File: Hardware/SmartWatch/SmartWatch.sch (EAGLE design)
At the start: 44 parts, among them U1 STM32L476, U3 UG-2828GDEDF11, U4 FAN5331SX, U5 APDS-9960, U6 LTC3557

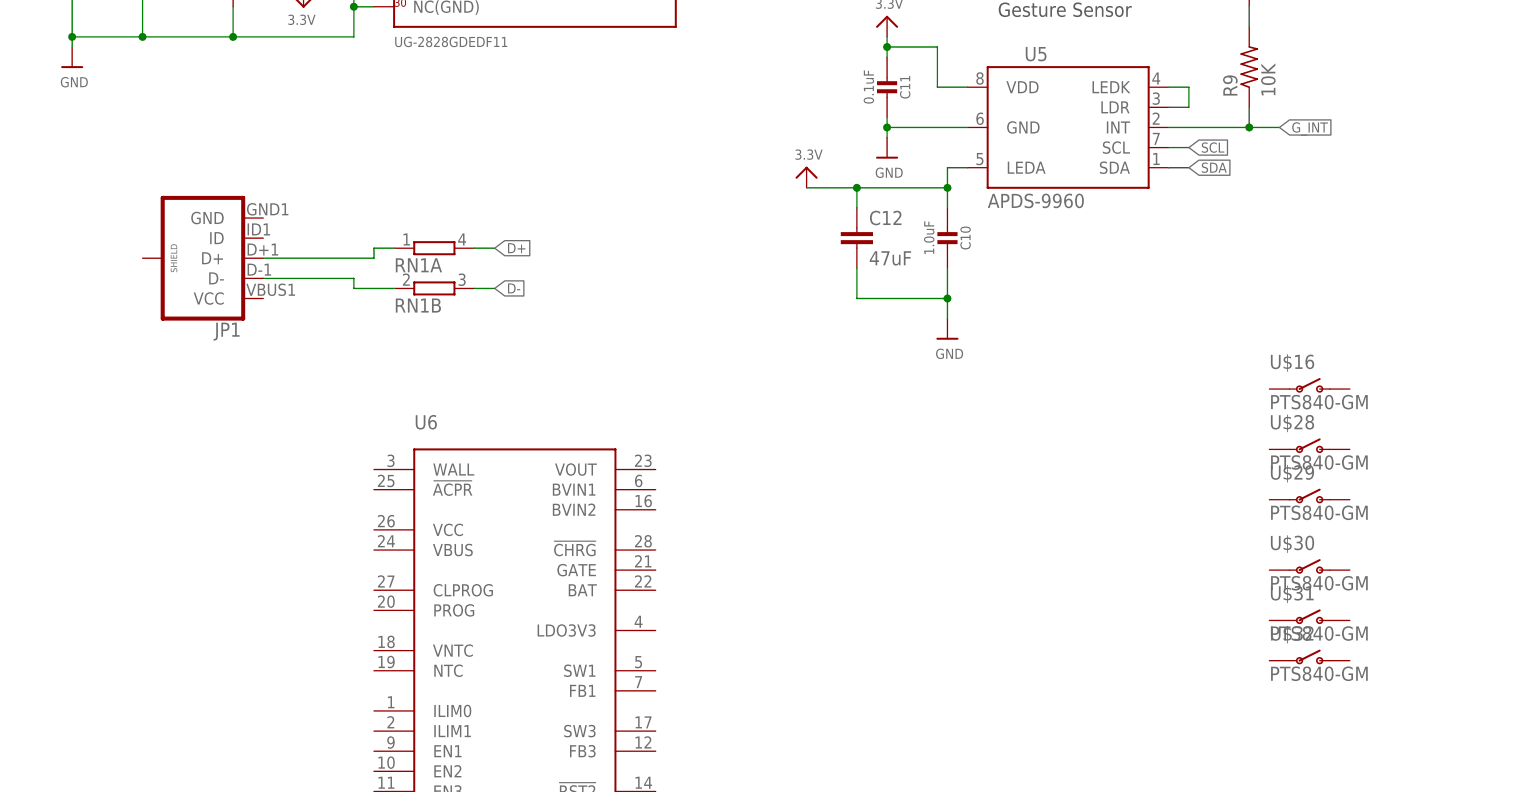
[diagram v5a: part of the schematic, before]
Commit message: created usb part
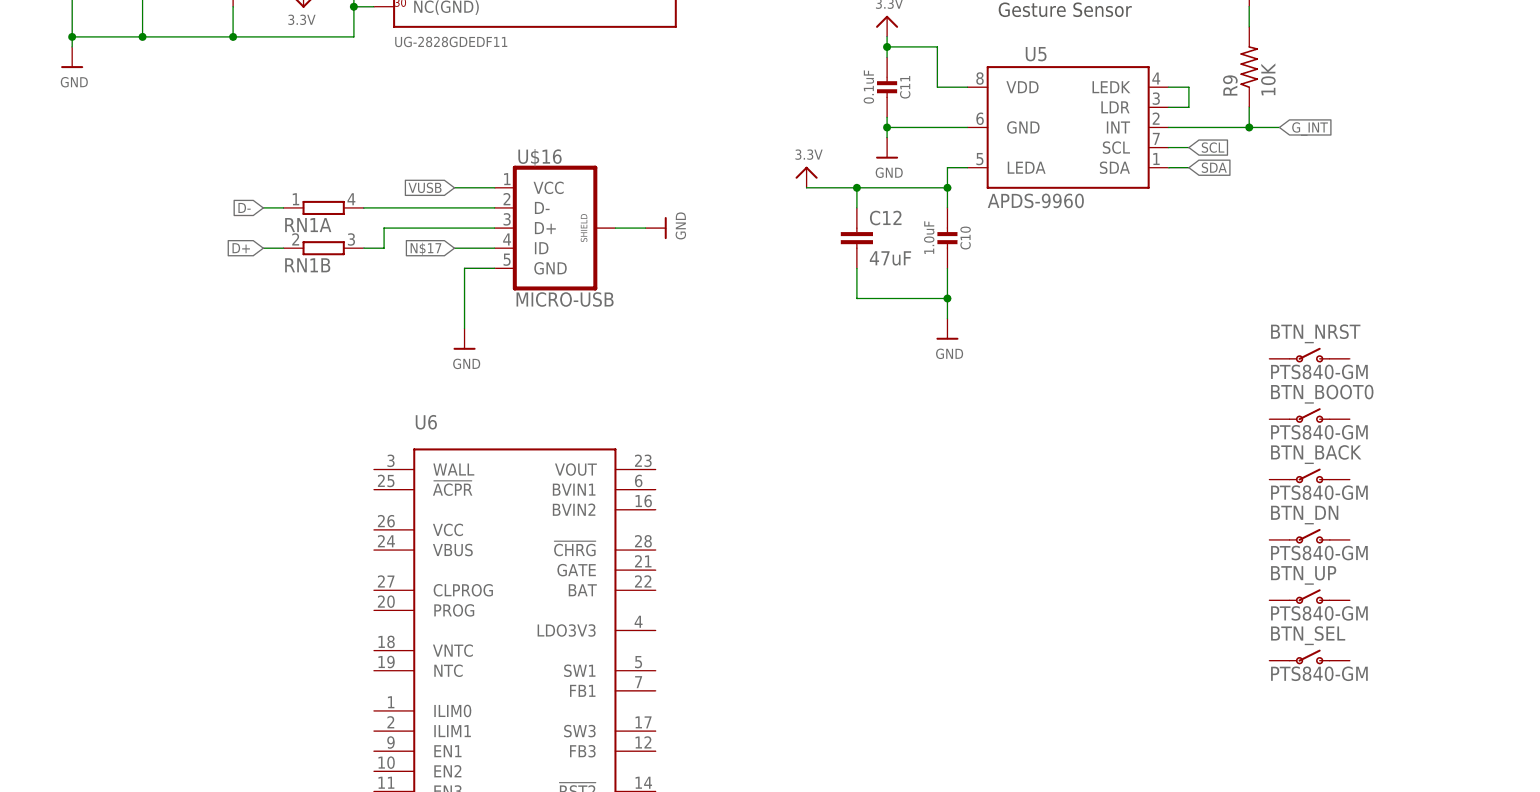
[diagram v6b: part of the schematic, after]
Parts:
- removed JP1: (no value), SparkFun-Connectors:USB_MICROB_PLUGCONN-11752
- removed U$28, U$29, U$30, U$31: PTS840-GM, SmartWatch:PTS840-GM
- added BTN_BACK, BTN_BOOT0, BTN_DN, BTN_NRST, BTN_UP: PTS840-GM, SmartWatch:PTS840-GM
- U$16: value PTS840-GM -> MICRO-USB; device SmartWatch:PTS840-GM -> SmartWatch:MICRO-USB
- renumbered U$32 to BTN_SEL
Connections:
- removed net N$10: JP1.D+, RN1A.1
- new net ID: RN1B.2, U$16.D+
- new net N$17: U$16.ID
- new net VUSB: U$16.VCC
- net D+: now also RN1B.1; no longer RN1A.2
- net D-: now also RN1A.1; no longer RN1B.2
- net GND: now also U$16.GND, U$16.SHIELD
- net N$15: now also RN1A.2, U$16.D-; no longer JP1.D-, RN1B.1
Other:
- moved on the sheet: RN1A, RN1B
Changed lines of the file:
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@@
 <part name="C1" library="microbuilder" deviceset="CAP_CERAMIC" device="0603MINI" value="1uF"/>
 <part name="U6" library="SmartWatch" deviceset="LTC3557" device=""/>
-<part name="JP1" library="SparkFun-Connectors" deviceset="USB_MICROB_PLUG" device="CONN-11752"/>
+<part name="U$27" library="supply1" deviceset="+12V" device="" value="+13V"/>
+<part name="BTN_NRST" library="SmartWatch" deviceset="PTS840-GM" device=""/>
+<part name="BTN_BOOT0" library="SmartWatch" deviceset="PTS840-GM" device=""/>
+<part name="BTN_BACK" library="SmartWatch" deviceset="PTS840-GM" device=""/>
+<part name="BTN_DN" library="SmartWatch" deviceset="PTS840-GM" device=""/>
+<part name="BTN_UP" library="SmartWatch" deviceset="PTS840-GM" device=""/>
+<part name="BTN_SEL" library="SmartWatch" deviceset="PTS840-GM" device=""/>
+<part name="U$16" library="SmartWatch" deviceset="MICRO-USB" device=""/>
+<part name="U$28" library="microbuilder" deviceset="GND" device=""/>
+<part name="U$29" library="microbuilder" deviceset="GND" device=""/>
 <part name="RN1" library="MicroBoard" deviceset="2R-N" device="EXBV4V"/>
-<part name="U$27" library="supply1" deviceset="+12V" device="" value="+13V"/>
-<part name="U$16" library="SmartWatch" deviceset="PTS840-GM" device=""/>
-<part name="U$28" library="SmartWatch" deviceset="PTS840-GM" device=""/>
-<part name="U$29" library="SmartWatch" deviceset="PTS840-GM" device=""/>
-<part name="U$30" library="SmartWatch" deviceset="PTS840-GM" device=""/>
-<part name="U$31" library="SmartWatch" deviceset="PTS840-GM" device=""/>
-<part name="U$32" library="SmartWatch" deviceset="PTS840-GM" device=""/>
 </parts>
 <sheets>
@@
 <instance part="C1" gate="G$1" x="13.97" y="69.85" rot="R180"/>
 <instance part="U6" gate="G$1" x="198.12" y="-48.26"/>
-<instance part="JP1" gate="G$1" x="158.75" y="1.27" rot="R180"/>
-<instance part="RN1" gate="A" x="187.96" y="2.54"/>
-<instance part="RN1" gate="B" x="187.96" y="-2.54"/>
 <instance part="U$27" gate="1" x="298.45" y="92.71"/>
-<instance part="U$16" gate="G$1" x="298.45" y="-15.24"/>
-<instance part="U$28" gate="G$1" x="298.45" y="-22.86"/>
-<instance part="U$29" gate="G$1" x="298.45" y="-29.21"/>
-<instance part="U$30" gate="G$1" x="298.45" y="-38.1"/>
-<instance part="U$31" gate="G$1" x="298.45" y="-44.45"/>
-<instance part="U$32" gate="G$1" x="298.45" y="-49.53"/>
+<instance part="BTN_NRST" gate="G$1" x="298.45" y="-11.43"/>
+<instance part="BTN_BOOT0" gate="G$1" x="298.45" y="-19.05"/>
+<instance part="BTN_BACK" gate="G$1" x="298.45" y="-26.67"/>
+<instance part="BTN_DN" gate="G$1" x="298.45" y="-34.29"/>
+<instance part="BTN_UP" gate="G$1" x="298.45" y="-41.91"/>
+<instance part="BTN_SEL" gate="G$1" x="298.45" y="-49.53"/>
+<instance part="U$16" gate="G$1" x="203.2" y="5.08"/>
+<instance part="U$28" gate="G$1" x="217.17" y="5.08" rot="R90"/>
+<instance part="U$29" gate="G$1" x="191.77" y="-10.16"/>
+<instance part="RN1" gate="A" x="173.99" y="7.62"/>
+<instance part="RN1" gate="B" x="173.99" y="2.54"/>
 </instances>
 <busses>
@@
 <pinref part="C12" gate="G$1" pin="2"/>
 </segment>
+<segment>
+<pinref part="U$28" gate="G$1" pin="GND"/>
+<pinref part="U$16" gate="G$1" pin="SHIELD"/>
+<wire x1="214.63" y1="5.08" x2="210.82" y2="5.08" width="0.1524" layer="91"/>
+</segment>
+<segment>
+<pinref part="U$16" gate="G$1" pin="GND"/>
+<wire x1="195.58" y1="0" x2="191.77" y2="0" width="0.1524" layer="91"/>
+<wire x1="191.77" y1="0" x2="191.77" y2="-7.62" width="0.1524" layer="91"/>
+<pinref part="U$29" gate="G$1" pin="GND"/>
+</segment>
 </net>
 <net name="BT_SCK" class="0">
@@
 </segment>
 </net>
-<net name="N$10" class="0">
-<segment>
-<pinref part="JP1" gate="G$1" pin="D+"/>
-<wire x1="166.37" y1="1.27" x2="180.34" y2="1.27" width="0.1524" layer="91"/>
-<wire x1="180.34" y1="1.27" x2="180.34" y2="2.54" width="0.1524" layer="91"/>
+<net name="VUSB" class="0">
+<segment>
+<pinref part="U$16" gate="G$1" pin="VCC"/>
+<wire x1="195.58" y1="10.16" x2="190.5" y2="10.16" width="0.1524" layer="91"/>
+<label x="190.5" y="10.16" size="1.27" layer="95" rot="R180" xref="yes"/>
+</segment>
+</net>
+<net name="N$15" class="0">
+<segment>
+<pinref part="U$16" gate="G$1" pin="D-"/>
+<pinref part="RN1" gate="A" pin="2"/>
+<wire x1="195.58" y1="7.62" x2="179.07" y2="7.62" width="0.1524" layer="91"/>
+</segment>
+</net>
+<net name="ID" class="0">
+<segment>
+<pinref part="U$16" gate="G$1" pin="D+"/>
+<wire x1="195.58" y1="5.08" x2="181.61" y2="5.08" width="0.1524" layer="91"/>
+<wire x1="181.61" y1="5.08" x2="181.61" y2="2.54" width="0.1524" layer="91"/>
+<pinref part="RN1" gate="B" pin="2"/>
+<wire x1="181.61" y1="2.54" x2="179.07" y2="2.54" width="0.1524" layer="91"/>
+</segment>
+</net>
+<net name="N$17" class="0">
+<segment>
+<pinref part="U$16" gate="G$1" pin="ID"/>
+<wire x1="195.58" y1="2.54" x2="190.5" y2="2.54" width="0.1524" layer="91"/>
+<label x="190.5" y="2.54" size="1.27" layer="95" rot="R180" xref="yes"/>
+</segment>
+</net>
+<net name="D-" class="0">
+<segment>
 <pinref part="RN1" gate="A" pin="1"/>
-<wire x1="180.34" y1="2.54" x2="182.88" y2="2.54" width="0.1524" layer="91"/>
-</segment>
-</net>
-<net name="N$15" class="0">
-<segment>
-<pinref part="JP1" gate="G$1" pin="D-"/>
-<wire x1="166.37" y1="-1.27" x2="177.8" y2="-1.27" width="0.1524" layer="91"/>
-<wire x1="177.8" y1="-1.27" x2="177.8" y2="-2.54" width="0.1524" layer="91"/>
+<wire x1="168.91" y1="7.62" x2="166.37" y2="7.62" width="0.1524" layer="91"/>
+<label x="166.37" y="7.62" size="1.27" layer="95" rot="R180" xref="yes"/>
+</segment>
+</net>
+<net name="D+" class="0">
+<segment>
 <pinref part="RN1" gate="B" pin="1"/>
-<wire x1="177.8" y1="-2.54" x2="182.88" y2="-2.54" width="0.1524" layer="91"/>
-</segment>
-</net>
-<net name="D+" class="0">
-<segment>
-<pinref part="RN1" gate="A" pin="2"/>
-<wire x1="193.04" y1="2.54" x2="195.58" y2="2.54" width="0.1524" layer="91"/>
-<label x="195.58" y="2.54" size="1.27" layer="95" xref="yes"/>
-</segment>
-</net>
-<net name="D-" class="0">
-<segment>
-<pinref part="RN1" gate="B" pin="2"/>
-<wire x1="193.04" y1="-2.54" x2="195.58" y2="-2.54" width="0.1524" layer="91"/>
-<label x="195.58" y="-2.54" size="1.27" layer="95" xref="yes"/>
-</segment>
-</net>
+<wire x1="168.91" y1="2.54" x2="166.37" y2="2.54" width="0.1524" layer="91"/>
+<label x="166.37" y="2.54" size="1.27" layer="95" rot="R180" xref="yes"/>
+</segment>
+</net>

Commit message: hardware updates
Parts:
- added C13, C15: 10uF, microbuilder:CAP_CERAMIC0603MINI
- added C16, C17: 2.2uF, microbuilder:CAP_CERAMIC0603MINI
- added R13, R14, R15, R16, R17, R18: 10K, resistor:R-US_R0603
- added R19: 2.5k, resistor:R-US_R0603
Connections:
- new net BNT_NRST: BTN_NRST.12, R13.2
- new net BTN_BACK: BTN_BACK.12, R15.2
- new net BTN_BOOT0: BTN_BOOT0.12, R14.2
- new net BTN_DN: BTN_DN.12, R16.2
- new net BTN_SEL: BTN_SEL.12, R18.2
- new net BTN_UP: BTN_UP.12, R17.2
- new net CHRG: U6.!CHRG
- new net N$10: RN1B.2, U$16.D-
- new net N$16: R19.2, U6.PROG
- new net N$19: C17.1, U6.BVIN1
- new net N$20: C16.1, U6.BVIN2
- new net VBAT: U6.BAT
- new net VOUT: C15.2, U6.VOUT
- net 3.3V: now also BTN_BACK.34, BTN_BOOT0.34, BTN_DN.34, BTN_NRST.34, BTN_SEL.34, BTN_UP.34
- net D+: now also RN1A.1; no longer RN1B.1
- net D-: now also RN1B.1; no longer RN1A.1
- net GND: now also C13.1, C15.1, C16.2, C17.2, R13.1, R14.1, R15.1, R16.1, R17.1, R18.1, R19.1, U6.GND, U6.NTC
- net ID: now also RN1A.2; no longer RN1B.2
- net N$15: now also C13.2, U6.VBUS; no longer RN1A.2, U$16.D-
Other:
- moved on the sheet: BTN_BACK, BTN_BOOT0, BTN_DN, BTN_NRST, BTN_SEL, BTN_UP, RN1A, RN1B

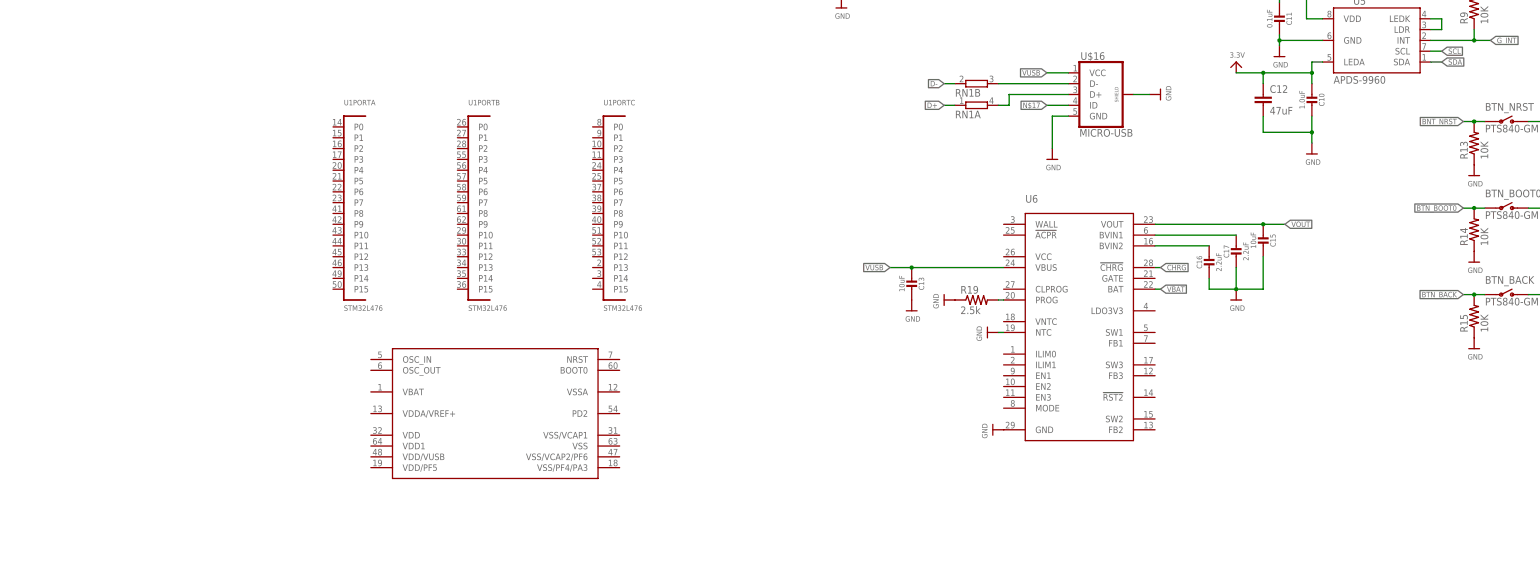
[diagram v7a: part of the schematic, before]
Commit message: added almost all parts, changed power management IC
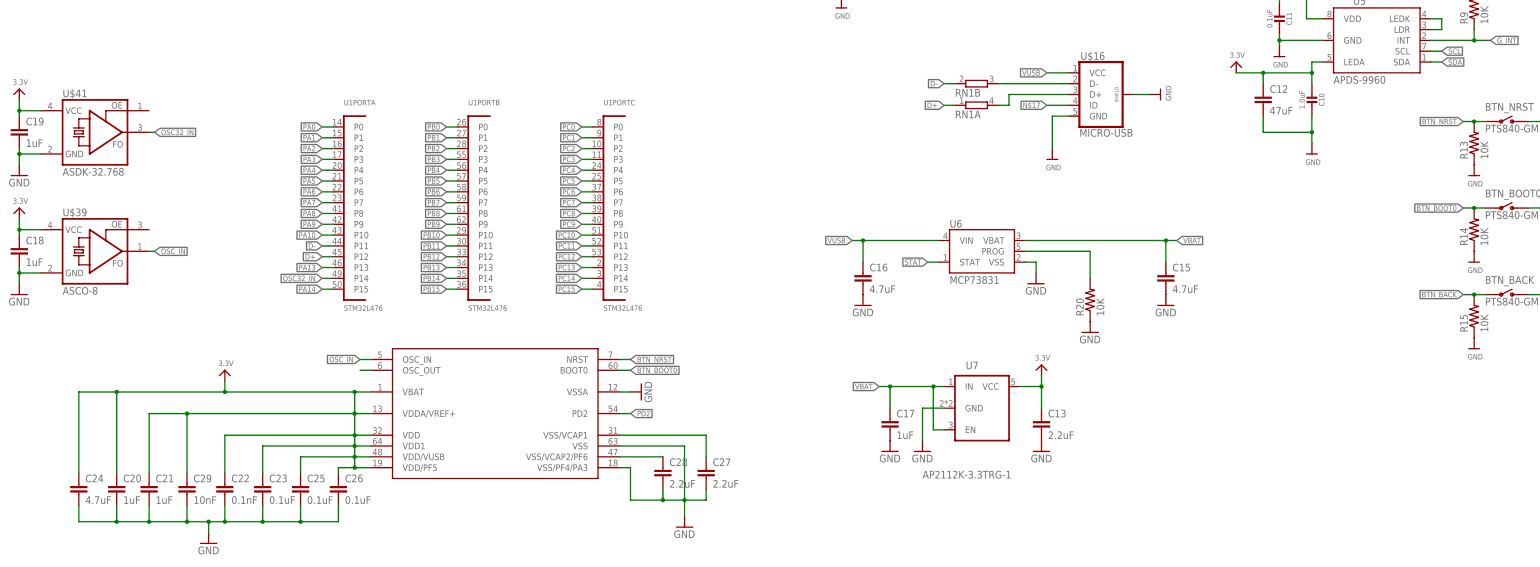
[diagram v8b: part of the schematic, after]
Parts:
- removed R19: 2.5k, resistor:R-US_R0603
- added C18, C19, C20, C21: 1uF, resistor:C-EUC0603
- added C22: 0.1nF, resistor:C-EUC0603
- added C23, C25, C26: 0.1uF, resistor:C-EUC0603
- added C24: 4.7uF, resistor:C-EUC0603
- added C27, C28: 2.2uF, resistor:C-EUC0603
- added C29: 10nF, resistor:C-EUC0603
- added R20: 10K, resistor:R-US_R0603
- added U$39: ASCO-8, SmartWatch:ASCO-8
- added U$41: ASDK-32.768, SmartWatch:ASDK-32.768
- added U7: AP2112K-3.3TRG-1, SparkFun-PowerIC:LDO-TPS78233
- C13: value 10uF -> 2.2uF; device microbuilder:CAP_CERAMIC0603MINI -> resistor:C-EUC0603
- C15: value 10uF -> 4.7uF; device microbuilder:CAP_CERAMIC0603MINI -> resistor:C-EUC0603; PROD_ID (none) -> CAP-08280
- C16: value 2.2uF -> 4.7uF; device microbuilder:CAP_CERAMIC0603MINI -> resistor:C-EUC0603; PROD_ID (none) -> CAP-08280
- C17: value 2.2uF -> 1uF; device microbuilder:CAP_CERAMIC0603MINI -> resistor:C-EUC0603; PROD_ID (none) -> CAP-00868
- U6: value LTC3557 -> MCP73831; device SmartWatch:LTC3557 -> SparkFun:MCP73831; PROD_ID (none) -> IC-09995
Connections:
- removed net BNT_NRST: BTN_NRST.12, R13.2
- removed net CHRG: U6.!CHRG
- removed net N$16: R19.2, U6.PROG
- removed net N$19: C17.1, U6.BVIN1
- removed net N$20: C16.1, U6.BVIN2
- removed net VOUT: C15.2, U6.VOUT
- new net BTN_NRST: BTN_NRST.12, R13.2, U1G$4.NRST
- new net N$27: C27.1, U1G$4.VSS/VCAP1
- new net N$29: C28.1, U1G$4.VSS/VCAP2/PF6
- new net OSC32_IN: U$41.FO, U1PORTA.P14
- new net OSC_IN: U$39.FO, U1G$4.OSC_IN
- new net PA0: U1PORTA.P0
- new net PA1: U1PORTA.P1
- new net PA10: U1PORTA.P10
- new net PA13: U1PORTA.P13
- new net PA14: U1PORTA.P15
- new net PA2: U1PORTA.P2
- new net PA3: U1PORTA.P3
- new net PA4: U1PORTA.P4
- new net PA5: U1PORTA.P5
- new net PA6: U1PORTA.P6
- new net PA7: U1PORTA.P7
- new net PA8: U1PORTA.P8
- new net PA9: U1PORTA.P9
- new net PB0: U1PORTB.P0
- new net PB1: U1PORTB.P1
- new net PB10: U1PORTB.P10
- new net PB11: U1PORTB.P11
- new net PB12: U1PORTB.P12
- new net PB13: U1PORTB.P13
- new net PB14: U1PORTB.P14
- new net PB15: U1PORTB.P15
- new net PB2: U1PORTB.P2
- new net PB3: U1PORTB.P3
- new net PB4: U1PORTB.P4
- new net PB5: U1PORTB.P5
- new net PB6: U1PORTB.P6
- new net PB7: U1PORTB.P7
- new net PB8: U1PORTB.P8
- new net PB9: U1PORTB.P9
- new net PC0: U1PORTC.P0
- new net PC1: U1PORTC.P1
- new net PC10: U1PORTC.P10
- new net PC11: U1PORTC.P11
- new net PC12: U1PORTC.P12
- new net PC13: U1PORTC.P13
- new net PC14: U1PORTC.P14
- new net PC15: U1PORTC.P15
- new net PC2: U1PORTC.P2
- new net PC3: U1PORTC.P3
- new net PC4: U1PORTC.P4
- new net PC5: U1PORTC.P5
- new net PC6: U1PORTC.P6
- new net PC7: U1PORTC.P7
- new net PC8: U1PORTC.P8
- new net PC9: U1PORTC.P9
- new net PD2: U1G$4.PD2
- new net PROG: R20.2, U6.PROG
- new net STAT: U6.STAT
- net 3.3V: now also C13.1, C18.1, C19.1, C20.1, C21.1, C22.1, C23.1, C24.1, C25.1, C26.1, C29.1, U$39.VCC, U$41.VCC, U1G$4.VBAT, U1G$4.VDD, U1G$4.VDD/PF5, U1G$4.VDD/VUSB, U1G$4.VDD1, U1G$4.VDDA/VREF+, U7.VCC
- net BTN_BOOT0: now also U1G$4.BOOT0
- net D+: now also U1PORTA.P12
- net D-: now also U1PORTA.P11
- net GND: now also C13.2, C15.2, C18.2, C19.2, C20.2, C21.2, C22.2, C23.2, C24.2, C25.2, C26.2, C27.2, C28.2, C29.2, R20.1, U$39.GND, U$41.GND, U1G$4.VSS, U1G$4.VSS/PF4/PA3, U1G$4.VSSA, U6.VSS, U7.GND; no longer C13.1, C15.1, R19.1, U6.GND, U6.NTC
- net N$15: now also U1G$4.OSC_OUT; no longer C13.2, U6.VBUS
- net VBAT: now also C15.1, C17.1, U6.VBAT, U7.EN, U7.IN; no longer U6.BAT
- net VUSB: now also C16.1, U6.VIN
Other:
- moved on the sheet: C13, C15, C16, C17
